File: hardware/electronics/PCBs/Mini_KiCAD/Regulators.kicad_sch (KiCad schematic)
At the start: 9 parts, among them U3 AP2202K-3.3, U4 AP2204K-1.8

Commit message: Rerouted the SPI devices and general cleanup, relocated all associated footprint library inside the project folder
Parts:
- REG.C.1, REG.C.2, REG.C.3, REG.C.4, REG.C.5, REG.C.6, REG.C.7: footprint Chip_Passives.PcbLib:0805 -> Chip_Passives.PcbLib:0805 - TALL
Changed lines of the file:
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@@
 			)
 		)
-		(property "Footprint" "Chip_Passives.PcbLib:0805"
+		(property "Footprint" "Chip_Passives.PcbLib:0805 - TALL"
 			(at 115.57 44.45 0)
 			(effects
@@
 			)
 		)
-		(property "Footprint" "Chip_Passives.PcbLib:0805"
+		(property "Footprint" "Chip_Passives.PcbLib:0805 - TALL"
 			(at 54.61 107.95 0)
 			(effects
@@
 			)
 		)
-		(property "Footprint" "Chip_Passives.PcbLib:0805"
+		(property "Footprint" "Chip_Passives.PcbLib:0805 - TALL"
 			(at 54.61 44.45 0)
 			(effects
@@
 			)
 		)
-		(property "Footprint" "Chip_Passives.PcbLib:0805"
+		(property "Footprint" "Chip_Passives.PcbLib:0805 - TALL"
 			(at 115.57 107.95 0)
 			(effects
@@
 			)
 		)
-		(property "Footprint" "Chip_Passives.PcbLib:0805"
+		(property "Footprint" "Chip_Passives.PcbLib:0805 - TALL"
 			(at 130.81 44.45 0)
 			(effects
@@
 			)
 		)
-		(property "Footprint" "Chip_Passives.PcbLib:0805"
+		(property "Footprint" "Chip_Passives.PcbLib:0805 - TALL"
 			(at 97.79 64.77 0)
 			(effects
@@
 			)
 		)
-		(property "Footprint" "Chip_Passives.PcbLib:0805"
+		(property "Footprint" "Chip_Passives.PcbLib:0805 - TALL"
 			(at 130.81 107.95 0)
 			(effects

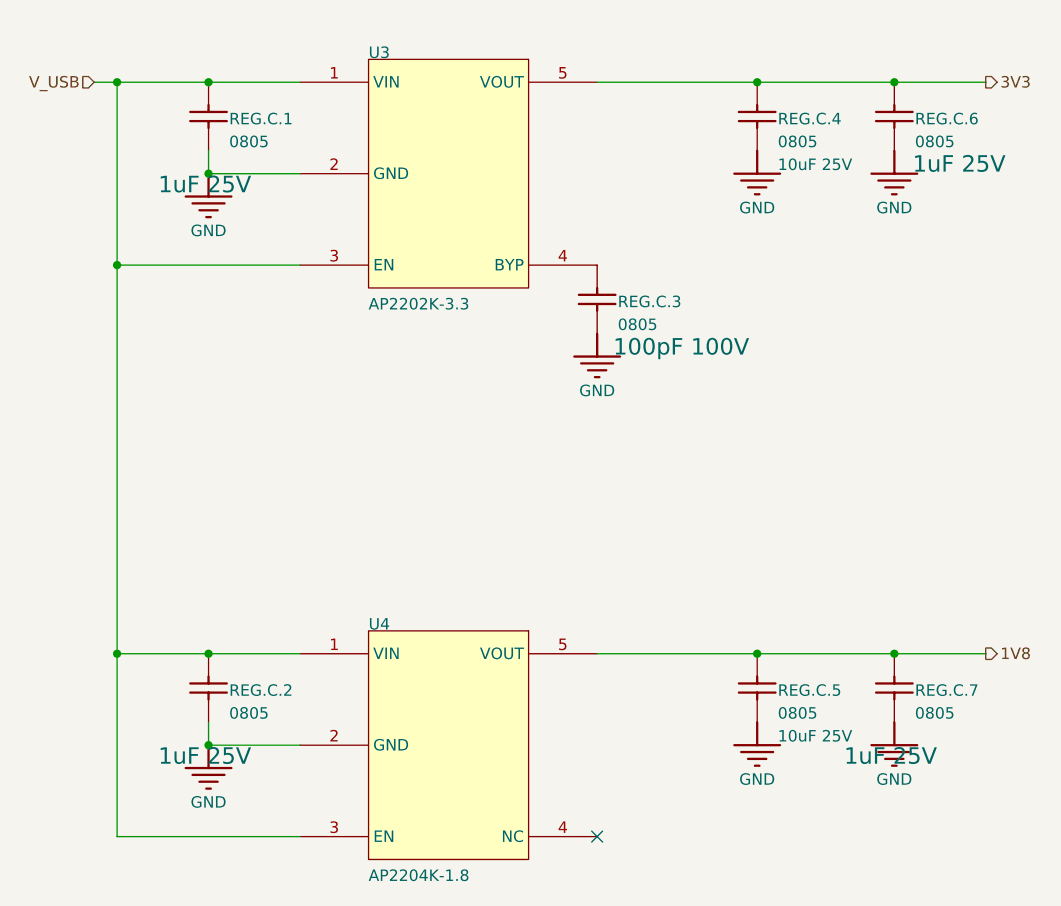
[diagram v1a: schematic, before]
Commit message: Changed button and SPI device pinout to be pin-compatible with the Ploopy Adept.
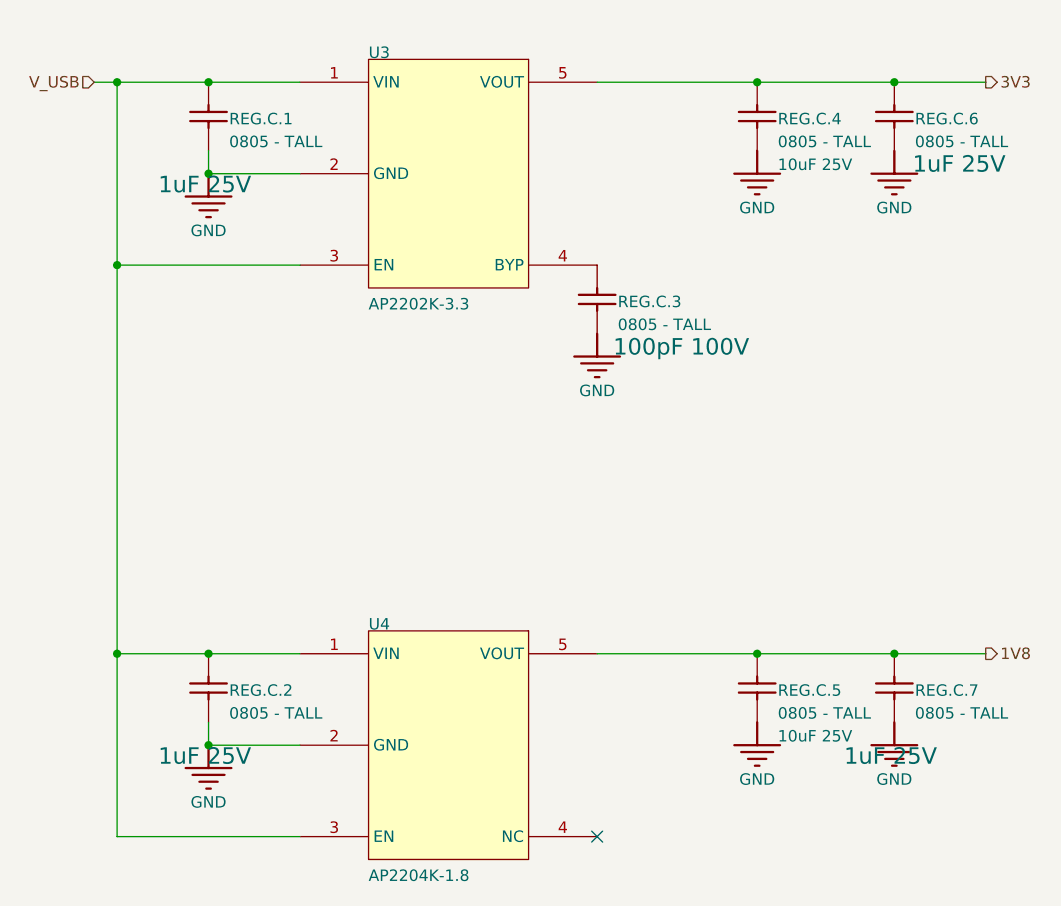
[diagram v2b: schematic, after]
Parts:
- REG.C.1, REG.C.2, REG.C.3, REG.C.4, REG.C.5, REG.C.6, REG.C.7: value 0805 -> 0805 - TALL
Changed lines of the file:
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@@
 			)
 		)
-		(property "Value" "0805"
+		(property "Value" "0805 - TALL"
 			(at 120.396 46.736 0)
 			(effects
@@
 			)
 		)
-		(property "Value" "0805"
+		(property "Value" "0805 - TALL"
 			(at 59.436 110.236 0)
 			(effects
@@
 			)
 		)
-		(property "Value" "0805"
+		(property "Value" "0805 - TALL"
 			(at 59.436 46.736 0)
 			(effects
@@
 			)
 		)
-		(property "Value" "0805"
+		(property "Value" "0805 - TALL"
 			(at 120.396 110.236 0)
 			(effects
@@
 			)
 		)
-		(property "Value" "0805"
+		(property "Value" "0805 - TALL"
 			(at 135.636 46.736 0)
 			(effects
@@
 			)
 		)
-		(property "Value" "0805"
+		(property "Value" "0805 - TALL"
 			(at 102.616 67.056 0)
 			(effects
@@
 			)
 		)
-		(property "Value" "0805"
+		(property "Value" "0805 - TALL"
 			(at 135.636 110.236 0)
 			(effects

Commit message: Replaced the AP2202K Voltage Regulator with easier to source AP2204K, and layout improvements for easier soldering.
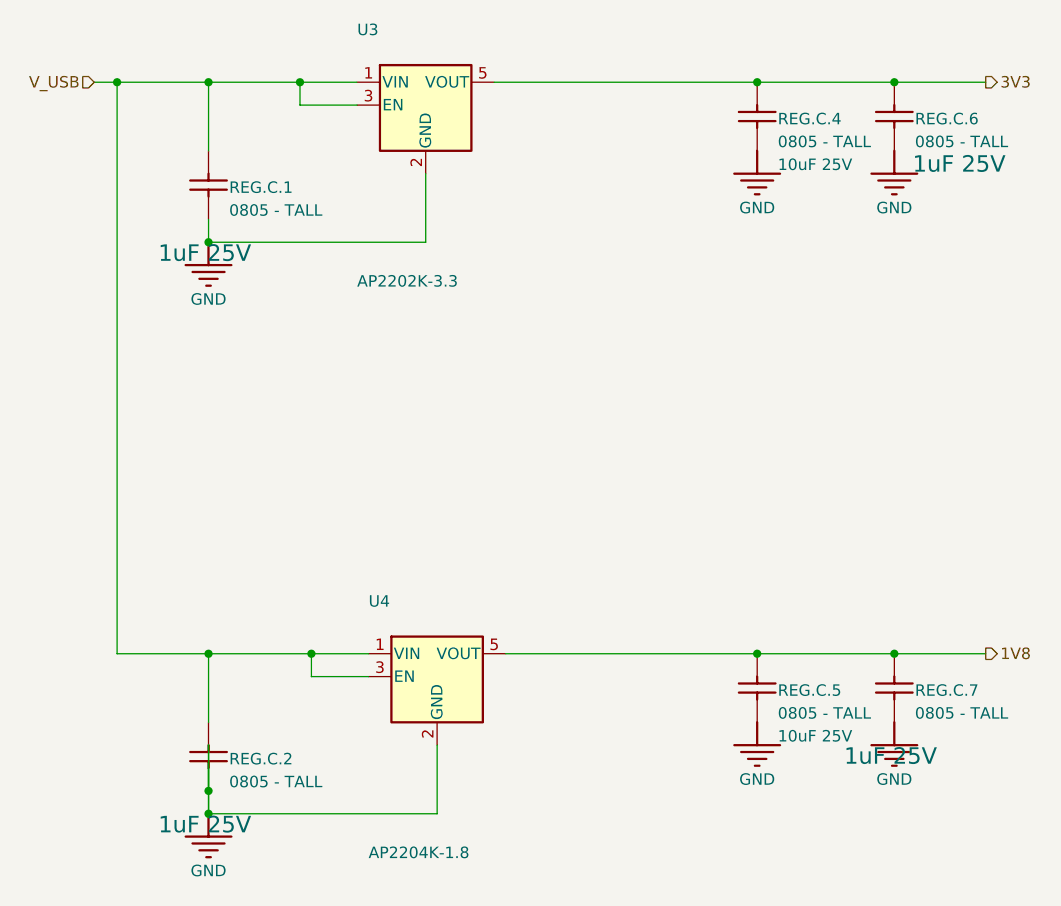
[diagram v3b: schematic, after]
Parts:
- removed REG.C.3: 0805 - TALL, Chip_Passives.PcbLib:0805 - TALL, symbol Mini-altium-import:MCU_1_Cap 0.1uF 100V
- U3: footprint PowerSupply:AP2202 - SOT95P270X145-5N -> Package_TO_SOT_SMD:SOT-23-5; symbol Base-altium-import:REG_0_AP2202K-3.3 -> Regulator_Linear:AP2204K-3.3
- U4: footprint PowerSupply:AP2202 - SOT95P270X145-5N -> Package_TO_SOT_SMD:SOT-23-5; symbol Base-altium-import:REG_0_AP2204K-1.8 -> Regulator_Linear:AP2204K-1.8
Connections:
- no-connect marks 1 -> 0
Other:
- moved on the sheet: REG.C.1, REG.C.2

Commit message: Resolved most DRC errors and re-annotated the schematic to be friendly to BOM generation.
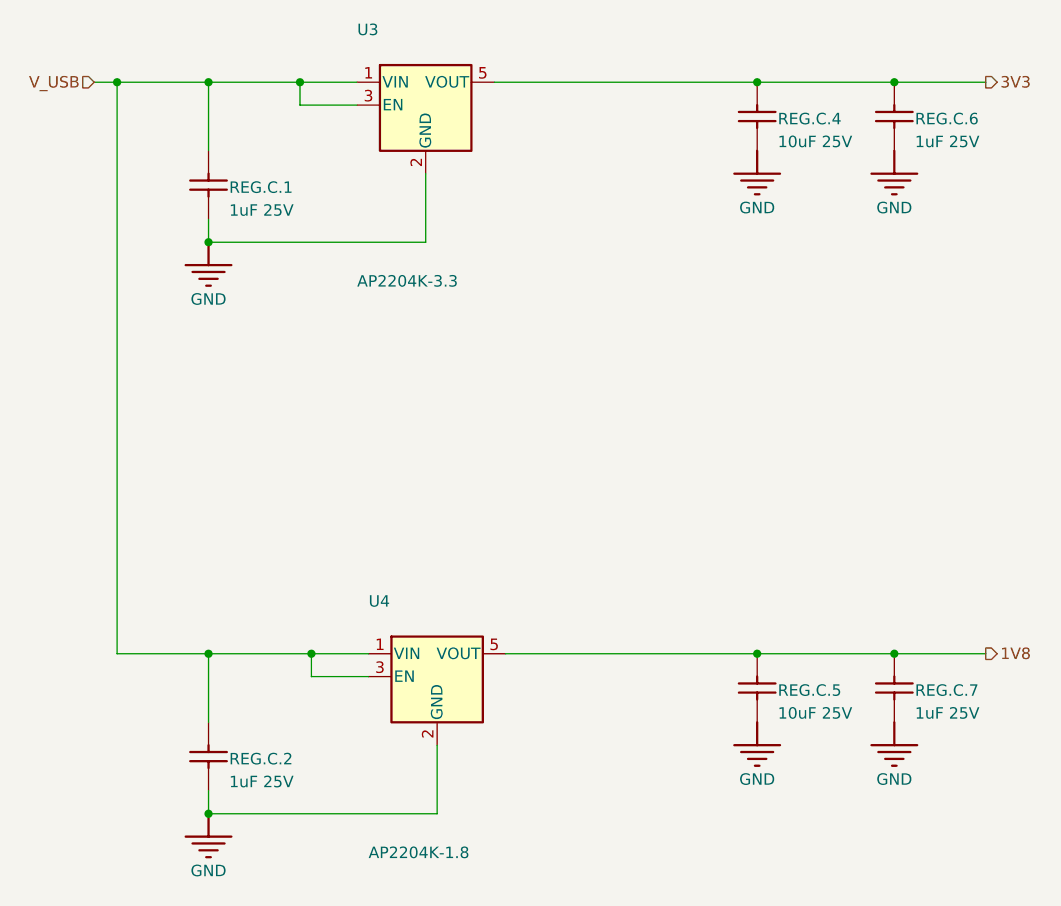
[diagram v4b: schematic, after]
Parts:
- REG.C.1, REG.C.2, REG.C.6, REG.C.7: value 0805 - TALL -> 1uF 25V
- REG.C.4, REG.C.5: value 0805 - TALL -> 10uF 25V
- U3: value AP2202K-3.3 -> AP2204K-3.3
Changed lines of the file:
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@@
 	)
 	(junction
-		(at 57.15 118.11)
-		(diameter 0)
-		(color 0 0 0 0)
-	)
-	(junction
 		(at 118.11 39.37)
 		(diameter 0)
@@
 	(wire
 		(pts
-			(xy 57.15 120.65) (xy 57.15 118.11)
-		)
-		(stroke
-			(width 0)
-			(type default)
-		)
-	)
-	(wire
-		(pts
 			(xy 73.66 41.91) (xy 67.31 41.91)
 		)
@@
 	(wire
 		(pts
-			(xy 57.15 118.11) (xy 57.15 113.03)
-		)
-		(stroke
-			(width 0.254)
-			(type default)
-		)
-	)
-	(wire
-		(pts
 			(xy 57.15 46.99) (xy 57.15 39.37)
 		)
@@
 	(wire
 		(pts
-			(xy 57.15 118.11) (xy 57.15 113.03)
-		)
-		(stroke
-			(width 0)
-			(type default)
-		)
-	)
-	(wire
-		(pts
 			(xy 68.58 105.41) (xy 68.58 102.87)
 		)
@@
 			)
 		)
-		(property "Value" "0805 - TALL"
+		(property "Value" "10uF 25V"
 			(at 120.396 46.736 0)
 			(effects
@@
 				)
 				(justify left bottom)
+				(hide yes)
 			)
 		)
@@
 			)
 		)
-		(property "Value" "0805 - TALL"
+		(property "Value" "1uF 25V"
 			(at 59.436 117.856 0)
 			(effects
@@
 				)
 				(justify left bottom)
+				(hide yes)
 			)
 		)
@@
 			)
 		)
-		(property "Value" "0805 - TALL"
+		(property "Value" "1uF 25V"
 			(at 59.436 54.356 0)
 			(effects
@@
 				)
 				(justify left bottom)
+				(hide yes)
 			)
 		)
@@
 			)
 		)
-		(property "Value" "AP2202K-3.3"
+		(property "Value" "AP2204K-3.3"
 			(at 73.66 62.23 0)
 			(effects
@@
 			)
 		)
-		(property "Value" "0805 - TALL"
+		(property "Value" "10uF 25V"
 			(at 120.396 110.236 0)
 			(effects
@@
 				)
 				(justify left bottom)
+				(hide yes)
 			)
 		)
@@
 			)
 		)
-		(property "Value" "0805 - TALL"
+		(property "Value" "1uF 25V"
 			(at 135.636 46.736 0)
 			(effects
@@
 				)
 				(justify left bottom)
+				(hide yes)
 			)
 		)
@@
 			)
 		)
-		(property "Value" "0805 - TALL"
+		(property "Value" "1uF 25V"
 			(at 135.636 110.236 0)
 			(effects
@@
 				)
 				(justify left bottom)
+				(hide yes)
 			)
 		)

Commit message: Rev1.002 Replaced all symbols in the schematic with built-in symbols where applicable. Reoriented the sensor to solve interference and tracking issues. Replaced the mid-mount USB port with regular port.
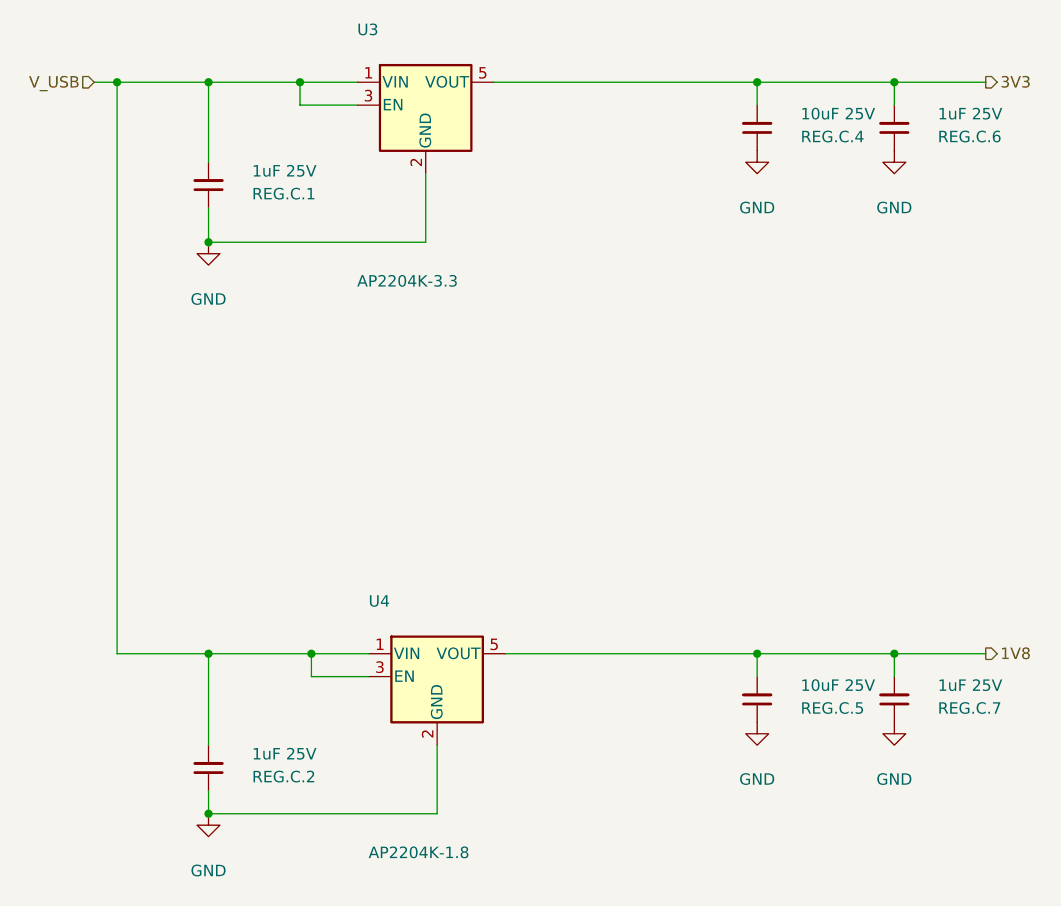
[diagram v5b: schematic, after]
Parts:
- REG.C.1, REG.C.2, REG.C.6, REG.C.7: symbol Mini-altium-import:MCU_1_Cap 0.1uF 100V -> Device:C_Small
- REG.C.4, REG.C.5: symbol Mini-altium-import:MOS_1_Cap 10uF 25V -> Device:C_Small
